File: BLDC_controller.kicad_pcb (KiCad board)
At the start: 4 copper layers, 50 x 38 mm, 368 parts, among them P2 CONN_01X06, P3 CONN_01X05, P5 CONN_01X05, Q1 PSMN2R0-30YLD, Q2 PSMN2R0-30YLD, Q3 PSMN2R0-30YLD, Q4 PSMN2R0-30YLD, Q5 PSMN2R0-30YLD, Q6 PSMN2R0-30YLD

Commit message: ready for 2nd review
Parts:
- moved REF** 0.35 mm to (178.3, 109.9)
- moved C19 0.32 mm to (176.8, 110.8)
- moved C5 0.30 mm to (176.7, 91.5)
- moved R14 0.25 mm to (163.5, 109.0)
- moved Q3 0.12 mm to (177.1, 105.4)
- moved Q5 0.08 mm to (177.1, 96.5)
- moved Q4 0.05 mm to (177.1, 105.4)
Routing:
- net +12V: track 32.3 -> 56.6 mm
- net /OUTU: track 47.4 -> 58.0 mm
- net /OUTW: track 32.9 -> 42.1 mm
- net /OUTV: track 29.1 -> 37.6 mm
- net GND: track 122.4 -> 118.4 mm
- net /LSW: track 21.0 -> 19.8 mm
- net /OSC_IN: track 7.60 -> 8.69 mm
- net /OP2P: track 6.87 -> 7.56 mm
- net +3V3: track 35.2 -> 34.6 mm
- net /V_ADC: track 18.7 -> 18.1 mm
- net /OP2N: track 13.4 -> 12.8 mm
- net /NRST: track 39.0 -> 38.5 mm
- net (no net): vias 4 -> 0

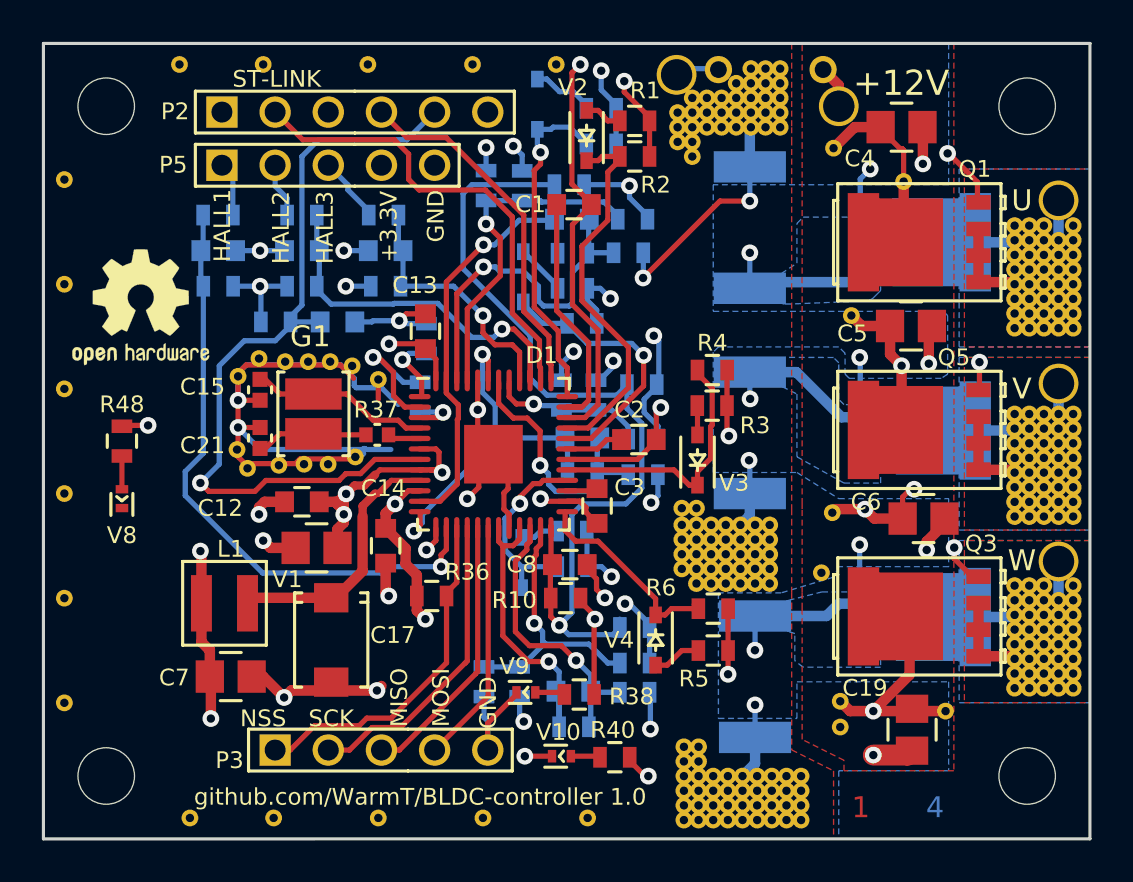
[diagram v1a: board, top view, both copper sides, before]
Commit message: board size changed to 49x32 mm
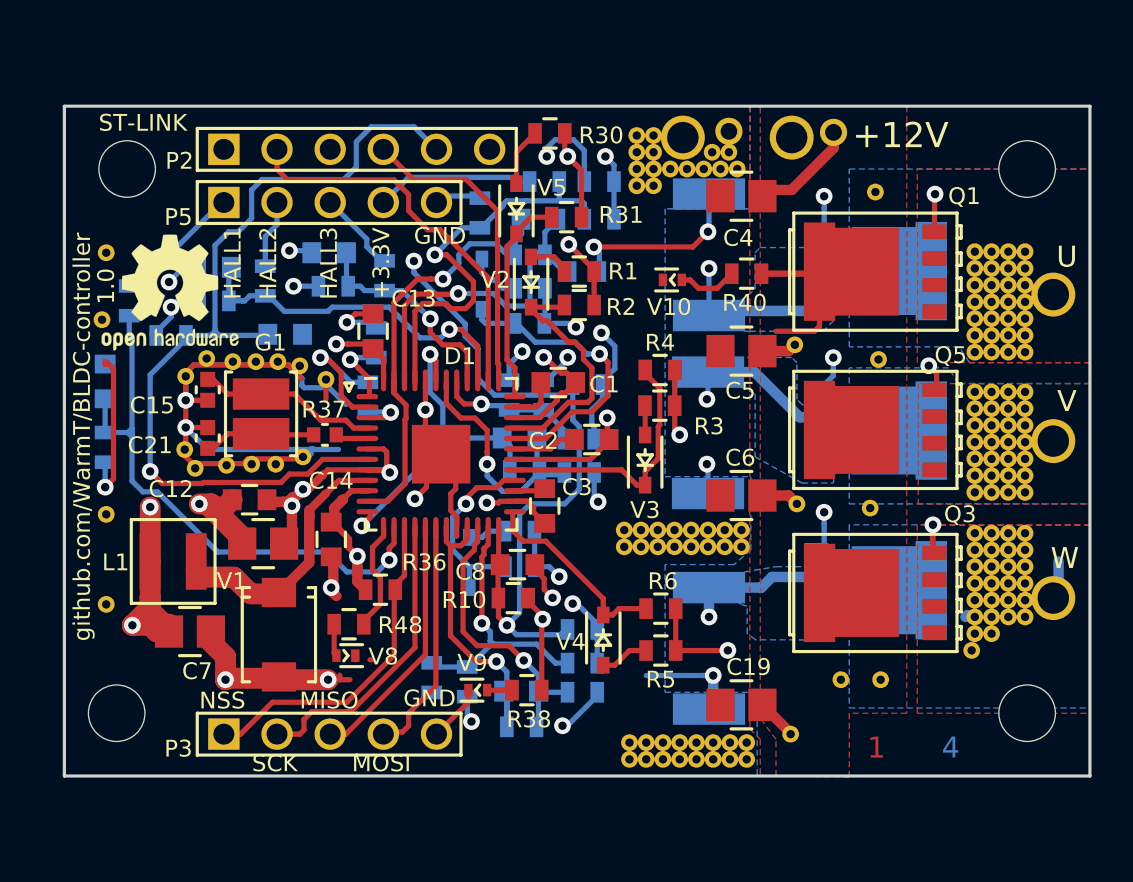
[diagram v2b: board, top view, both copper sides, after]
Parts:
- removed the REF** at (176.3, 84.6)
- removed the REF** at (183.8, 96.4)
- removed the REF** at (183.1, 96.4)
- removed the REF** at (182.3, 96.4)
- removed the REF** at (181.7, 96.4)
- removed the REF** at (184.4, 95.7)
- removed the REF** at (183.8, 95.7)
- removed the REF** at (183.1, 95.7)
- removed the REF** at (182.3, 95.7)
- removed the REF** at (181.7, 103.9)
- removed the REF** at (184.4, 91.6)
- removed the REF** at (161.2, 115.0)
- removed the REF** at (183.8, 91.6)
- removed the REF** at (183.1, 91.6)
- removed the REF** at (182.3, 91.6)
- removed the REF** at (181.7, 91.6)
- removed the REF** at (184.4, 90.9)
- removed the REF** at (183.8, 90.9)
- removed the REF** at (183.1, 90.9)
- removed the REF** at (182.3, 90.9)
- removed the REF** at (181.7, 90.9)
- removed the REF** at (184.4, 90.2)
- removed the REF** at (159.8, 79.0)
- removed the REF** at (183.8, 90.2)
- removed the REF** at (183.1, 90.2)
- removed the REF** at (182.3, 90.2)
- removed the REF** at (181.7, 90.2)
- removed the REF** at (184.4, 89.5)
- removed the REF** at (183.8, 89.5)
- removed the REF** at (183.1, 89.5)
- removed the REF** at (182.3, 89.5)
- removed the REF** at (181.7, 89.5)
- removed the REF** at (184.4, 88.8)
- removed the REF** at (136.2, 109.5)
- removed the REF** at (183.8, 88.8)
- removed the REF** at (183.1, 88.8)
- removed the REF** at (182.3, 88.8)
- removed the REF** at (181.7, 88.8)
- removed the REF** at (184.4, 88.1)
- removed the REF** at (183.8, 88.1)
- removed the REF** at (183.1, 88.1)
- removed the REF** at (182.3, 88.1)
- removed the REF** at (181.7, 88.1)
- removed the REF** at (184.4, 87.4)
- removed the REF** at (155.8, 79.0)
- removed the REF** at (183.8, 87.4)
- removed the REF** at (183.1, 87.4)
- removed the REF** at (182.3, 87.4)
- removed the REF** at (181.7, 87.4)
- removed the REF** at (181.7, 95.7)
- removed the REF** at (184.4, 86.7)
- removed the REF** at (183.1, 86.7)
- removed the REF** at (182.3, 86.7)
- removed the REF** at (181.7, 86.7)
- removed the REF** at (166.2, 83.4)
- removed the REF** at (150.8, 79.0)
- removed the REF** at (166.4, 100.2)
- removed the REF** at (165.8, 100.2)
- removed the REF** at (170.4, 82.0)
- removed the REF** at (169.8, 82.0)
- removed the REF** at (169.1, 82.0)
- removed the REF** at (168.3, 82.0)
- removed the REF** at (167.7, 82.0)
- removed the REF** at (166.9, 82.0)
- removed the REF** at (166.2, 82.0)
- removed the REF** at (165.6, 82.0)
- removed the REF** at (145.8, 79.0)
- removed the REF** at (170.4, 81.3)
- removed the REF** at (169.8, 81.3)
- removed the REF** at (169.1, 81.3)
- removed the REF** at (168.3, 81.3)
- removed the REF** at (167.7, 81.3)
- removed the REF** at (166.9, 81.3)
- removed the REF** at (166.2, 81.3)
- removed the REF** at (165.6, 81.3)
- removed the REF** at (170.4, 80.6)
- removed the REF** at (169.8, 80.6)
- removed the REF** at (141.8, 79.0)
- removed the REF** at (169.1, 80.6)
- removed the REF** at (168.3, 80.6)
- removed the REF** at (167.7, 80.6)
- removed the REF** at (166.9, 80.6)
- removed the REF** at (166.2, 80.6)
- removed the REF** at (170.4, 79.9)
- removed the REF** at (169.8, 79.9)
- removed the REF** at (169.1, 79.9)
- removed the REF** at (168.3, 79.9)
- removed the REF** at (166.2, 82.7)
- removed the REF** at (136.2, 84.5)
- removed the REF** at (165.6, 82.7)
- removed the REF** at (170.4, 79.2)
- removed the REF** at (169.8, 79.2)
- removed the REF** at (169.1, 79.2)
- removed the REF** at (166.6, 112.3)
- removed the REF** at (165.8, 112.3)
- removed the REF** at (166.6, 111.6)
- removed the REF** at (165.8, 111.6)
- removed the REF** at (169.9, 103.8)
- removed the REF** at (169.2, 103.8)
- removed the REF** at (168.6, 103.8)
- removed the REF** at (167.8, 103.8)
- removed the REF** at (167.2, 103.8)
- removed the REF** at (166.4, 103.8)
- removed the REF** at (169.9, 103.1)
- removed the REF** at (169.2, 103.1)
- removed the REF** at (168.6, 103.1)
- removed the REF** at (167.8, 103.1)
- removed the REF** at (167.2, 103.1)
- removed the REF** at (166.4, 103.1)
- removed the REF** at (169.9, 101.0)
- removed the REF** at (165.8, 103.1)
- removed the REF** at (169.9, 102.4)
- removed the REF** at (169.2, 102.4)
- removed the REF** at (168.6, 102.4)
- removed the REF** at (167.8, 102.4)
- removed the REF** at (167.2, 102.4)
- removed the REF** at (166.4, 102.4)
- removed the REF** at (165.8, 102.4)
- removed the REF** at (169.9, 101.7)
- removed the REF** at (169.2, 101.7)
- removed the REF** at (168.6, 101.7)
- removed the REF** at (167.8, 101.7)
- removed the REF** at (167.2, 101.7)
- removed the REF** at (166.4, 101.7)
- removed the REF** at (165.8, 101.7)
- removed the REF** at (169.2, 101.0)
- removed the REF** at (168.6, 101.0)
- removed the REF** at (167.8, 101.0)
- removed the REF** at (167.2, 101.0)
- removed the REF** at (165.8, 101.0)
- removed the REF** at (171.4, 115.1)
- removed the REF** at (170.8, 115.1)
- removed the REF** at (170.1, 115.1)
- removed the REF** at (169.3, 115.1)
- removed the REF** at (168.7, 115.1)
- removed the REF** at (167.9, 115.1)
- removed the REF** at (167.2, 115.1)
- removed the REF** at (166.6, 115.1)
- removed the REF** at (165.8, 115.1)
- removed the REF** at (142.2, 115.0)
- removed the REF** at (171.4, 114.4)
- removed the REF** at (170.8, 114.4)
- removed the REF** at (170.1, 114.4)
- removed the REF** at (169.3, 114.4)
- removed the REF** at (168.7, 114.4)
- removed the REF** at (167.9, 114.4)
- removed the REF** at (167.2, 114.4)
- removed the REF** at (166.6, 114.4)
- removed the REF** at (165.8, 114.4)
- removed the REF** at (171.4, 113.7)
- removed the REF** at (146.2, 115.0)
- removed the REF** at (170.8, 113.7)
- removed the REF** at (170.1, 113.7)
- removed the REF** at (169.3, 113.7)
- removed the REF** at (168.7, 113.7)
- removed the REF** at (167.9, 113.7)
- removed the REF** at (167.2, 113.7)
- removed the REF** at (166.6, 113.7)
- removed the REF** at (165.8, 113.7)
- removed the REF** at (171.4, 113.0)
- removed the REF** at (170.8, 113.0)
- removed the REF** at (151.2, 115.0)
- removed the REF** at (170.1, 113.0)
- removed the REF** at (169.3, 113.0)
- removed the REF** at (168.7, 113.0)
- removed the REF** at (167.9, 113.0)
- removed the REF** at (167.2, 113.0)
- removed the REF** at (166.6, 113.0)
- removed the REF** at (156.2, 115.0)
- removed the REF** at (173.0, 83.0)
- removed the REF** at (172.9, 100.4)
- removed the REF** at (172.4, 103.3)
- removed the REF** at (173.8, 91.0)
- removed the REF** at (173.3, 110.7)
- removed the REF** at (184.4, 108.8)
- removed the REF** at (183.8, 108.8)
- removed the REF** at (183.1, 108.8)
- removed the REF** at (182.3, 108.8)
- removed the REF** at (181.7, 108.8)
- removed the REF** at (184.4, 108.1)
- removed the REF** at (183.8, 108.1)
- removed the REF** at (183.1, 108.1)
- removed the REF** at (182.3, 108.1)
- removed the REF** at (181.7, 108.1)
- removed the REF** at (184.4, 107.4)
- removed the REF** at (183.8, 107.4)
- removed the REF** at (183.1, 107.4)
- removed the REF** at (182.3, 107.4)
- removed the REF** at (181.7, 107.4)
- removed the REF** at (184.4, 106.7)
- removed the REF** at (183.8, 106.7)
- removed the REF** at (183.1, 106.7)
- removed the REF** at (182.3, 106.7)
- removed the REF** at (181.7, 106.7)
- removed the REF** at (184.4, 106.0)
- removed the REF** at (183.8, 106.0)
- removed the REF** at (183.1, 106.0)
- removed the REF** at (182.3, 106.0)
- removed the REF** at (181.7, 106.0)
- removed the REF** at (184.4, 105.3)
- removed the REF** at (183.8, 105.3)
- removed the REF** at (183.1, 105.3)
- removed the REF** at (182.3, 105.3)
- removed the REF** at (181.7, 105.3)
- removed the REF** at (184.4, 104.6)
- removed the REF** at (183.8, 104.6)
- removed the REF** at (183.1, 104.6)
- removed the REF** at (182.3, 104.6)
- removed the REF** at (181.7, 104.6)
- removed the REF** at (184.4, 103.9)
- removed the REF** at (183.1, 103.9)
- removed the REF** at (182.3, 103.9)
- removed the REF** at (184.4, 100.6)
- removed the REF** at (183.8, 100.6)
- removed the REF** at (183.1, 100.6)
- removed the REF** at (182.3, 100.6)
- removed the REF** at (181.7, 100.6)
- removed the REF** at (184.4, 99.9)
- removed the REF** at (183.8, 99.9)
- removed the REF** at (183.1, 99.9)
- removed the REF** at (182.3, 99.9)
- removed the REF** at (181.7, 99.9)
- removed the REF** at (184.4, 99.2)
- removed the REF** at (178.3, 109.9)
- removed the REF** at (183.8, 99.2)
- removed the REF** at (183.1, 99.2)
- removed the REF** at (182.3, 99.2)
- removed the REF** at (181.7, 99.2)
- removed the REF** at (184.4, 98.5)
- removed the REF** at (183.8, 98.5)
- removed the REF** at (183.1, 98.5)
- removed the REF** at (182.3, 98.5)
- removed the REF** at (181.7, 98.5)
- removed the REF** at (184.4, 97.8)
- removed the REF** at (173.3, 109.4)
- removed the REF** at (183.8, 97.8)
- removed the REF** at (183.1, 97.8)
- removed the REF** at (182.3, 97.8)
- removed the REF** at (181.7, 97.8)
- removed the REF** at (184.4, 97.1)
- removed the REF** at (183.8, 97.1)
- removed the REF** at (183.1, 97.1)
- removed the REF** at (182.3, 97.1)
- removed the REF** at (181.7, 97.1)
- removed the REF** at (184.4, 96.4)
- added REF**: VIA-0.8mm-0.4mm, project_footprints:VIA-0.8mm-0.4mm, F.Cu at (175.0, 85.1)
- added REF**: VIA-0.8mm-0.4mm, project_footprints:VIA-0.8mm-0.4mm, F.Cu at (168.4, 84.0)
- added REF**: VIA-0.8mm-0.4mm, project_footprints:VIA-0.8mm-0.4mm, F.Cu at (179.8, 103.8)
- added REF**: VIA-0.8mm-0.4mm, project_footprints:VIA-0.8mm-0.4mm, F.Cu at (182.2, 103.0)
- added REF**: VIA-0.8mm-0.4mm, project_footprints:VIA-0.8mm-0.4mm, F.Cu at (181.3, 103.0)
- added REF**: VIA-0.8mm-0.4mm, project_footprints:VIA-0.8mm-0.4mm, F.Cu at (180.6, 103.0)
- added REF**: VIA-0.8mm-0.4mm, project_footprints:VIA-0.8mm-0.4mm, F.Cu at (179.8, 103.0)
- added REF**: VIA-0.8mm-0.4mm, project_footprints:VIA-0.8mm-0.4mm, F.Cu at (182.2, 102.2)
- added REF**: VIA-0.8mm-0.4mm, project_footprints:VIA-0.8mm-0.4mm, F.Cu at (181.3, 102.2)
- added REF**: VIA-0.8mm-0.4mm, project_footprints:VIA-0.8mm-0.4mm, F.Cu at (180.6, 102.2)
- added REF**: VIA-0.8mm-0.4mm, project_footprints:VIA-0.8mm-0.4mm, F.Cu at (179.8, 102.2)
- added REF**: VIA-0.8mm-0.4mm, project_footprints:VIA-0.8mm-0.4mm, F.Cu at (182.2, 101.4)
- added REF**: VIA-0.8mm-0.4mm, project_footprints:VIA-0.8mm-0.4mm, F.Cu at (167.6, 84.0)
- added REF**: VIA-0.8mm-0.4mm, project_footprints:VIA-0.8mm-0.4mm, F.Cu at (181.3, 101.4)
- added REF**: VIA-0.8mm-0.4mm, project_footprints:VIA-0.8mm-0.4mm, F.Cu at (180.6, 101.4)
- added REF**: VIA-0.8mm-0.4mm, project_footprints:VIA-0.8mm-0.4mm, F.Cu at (168.8, 112.2)
- added REF**: VIA-0.8mm-0.4mm, project_footprints:VIA-0.8mm-0.4mm, F.Cu at (168.1, 112.2)
- added REF**: VIA-0.8mm-0.4mm, project_footprints:VIA-0.8mm-0.4mm, F.Cu at (167.2, 112.2)
- added REF**: VIA-0.8mm-0.4mm, project_footprints:VIA-0.8mm-0.4mm, F.Cu at (166.4, 112.2)
- added REF**: VIA-0.8mm-0.4mm, project_footprints:VIA-0.8mm-0.4mm, F.Cu at (165.7, 112.2)
- added REF**: VIA-0.8mm-0.4mm, project_footprints:VIA-0.8mm-0.4mm, F.Cu at (164.8, 112.2)
- added REF**: VIA-0.8mm-0.4mm, project_footprints:VIA-0.8mm-0.4mm, F.Cu at (164.1, 112.2)
- added REF**: VIA-0.8mm-0.4mm, project_footprints:VIA-0.8mm-0.4mm, F.Cu at (163.2, 112.2)
- added REF**: VIA-0.8mm-0.4mm, project_footprints:VIA-0.8mm-0.4mm, F.Cu at (166.8, 84.0)
- added REF**: VIA-0.8mm-0.4mm, project_footprints:VIA-0.8mm-0.4mm, F.Cu at (168.8, 111.4)
- added REF**: VIA-0.8mm-0.4mm, project_footprints:VIA-0.8mm-0.4mm, F.Cu at (168.1, 111.4)
- added REF**: VIA-0.8mm-0.4mm, project_footprints:VIA-0.8mm-0.4mm, F.Cu at (167.2, 111.4)
- added REF**: VIA-0.8mm-0.4mm, project_footprints:VIA-0.8mm-0.4mm, F.Cu at (166.4, 111.4)
- added REF**: VIA-0.8mm-0.4mm, project_footprints:VIA-0.8mm-0.4mm, F.Cu at (165.7, 111.4)
- added REF**: VIA-0.8mm-0.4mm, project_footprints:VIA-0.8mm-0.4mm, F.Cu at (164.8, 111.4)
- added REF**: VIA-0.8mm-0.4mm, project_footprints:VIA-0.8mm-0.4mm, F.Cu at (164.1, 111.4)
- added REF**: VIA-0.8mm-0.4mm, project_footprints:VIA-0.8mm-0.4mm, F.Cu at (170.9, 111.0)
- added REF**: VIA-0.8mm-0.4mm, project_footprints:VIA-0.8mm-0.4mm, F.Cu at (173.3, 108.4)
- added REF**: VIA-0.8mm-0.4mm, project_footprints:VIA-0.8mm-0.4mm, F.Cu at (175.2, 108.4)
- added REF**: VIA-0.8mm-0.4mm, project_footprints:VIA-0.8mm-0.4mm, F.Cu at (166.0, 84.0)
- added REF**: VIA-0.8mm-0.4mm, project_footprints:VIA-0.8mm-0.4mm, F.Cu at (174.8, 100.2)
- added REF**: VIA-0.8mm-0.4mm, project_footprints:VIA-0.8mm-0.4mm, F.Cu at (175.2, 93.1)
- added REF**: VIA-0.8mm-0.4mm, project_footprints:VIA-0.8mm-0.4mm, F.Cu at (171.2, 92.4)
- added REF**: VIA-0.8mm-0.4mm, project_footprints:VIA-0.8mm-0.4mm, F.Cu at (171.2, 100.0)
- added REF**: VIA-0.8mm-0.4mm, project_footprints:VIA-0.8mm-0.4mm, F.Cu at (179.8, 101.4)
- added REF**: VIA-0.8mm-0.4mm, project_footprints:VIA-0.8mm-0.4mm, F.Cu at (179.8, 94.7)
- added REF**: VIA-0.8mm-0.4mm, project_footprints:VIA-0.8mm-0.4mm, F.Cu at (179.8, 88.0)
- added REF**: VIA-0.8mm-0.4mm, project_footprints:VIA-0.8mm-0.4mm, F.Cu at (165.2, 84.0)
- added REF**: VIA-0.8mm-0.4mm, project_footprints:VIA-0.8mm-0.4mm, F.Cu at (164.4, 84.0)
- added REF**: VIA-0.8mm-0.4mm, project_footprints:VIA-0.8mm-0.4mm, F.Cu at (163.6, 84.0)
- added REF**: VIA-0.8mm-0.4mm, project_footprints:VIA-0.8mm-0.4mm, F.Cu at (168.6, 102.0)
- added REF**: VIA-0.8mm-0.4mm, project_footprints:VIA-0.8mm-0.4mm, F.Cu at (167.8, 102.0)
- added REF**: VIA-0.8mm-0.4mm, project_footprints:VIA-0.8mm-0.4mm, F.Cu at (167.0, 102.0)
- added REF**: VIA-0.8mm-0.4mm, project_footprints:VIA-0.8mm-0.4mm, F.Cu at (164.4, 82.4)
- added REF**: VIA-0.8mm-0.4mm, project_footprints:VIA-0.8mm-0.4mm, F.Cu at (166.2, 102.0)
- added REF**: VIA-0.8mm-0.4mm, project_footprints:VIA-0.8mm-0.4mm, F.Cu at (165.4, 102.0)
- added REF**: VIA-0.8mm-0.4mm, project_footprints:VIA-0.8mm-0.4mm, F.Cu at (164.6, 102.0)
- added REF**: VIA-0.8mm-0.4mm, project_footprints:VIA-0.8mm-0.4mm, F.Cu at (163.8, 102.0)
- added REF**: VIA-0.8mm-0.4mm, project_footprints:VIA-0.8mm-0.4mm, F.Cu at (163.0, 102.0)
- added REF**: VIA-0.8mm-0.4mm, project_footprints:VIA-0.8mm-0.4mm, F.Cu at (168.6, 101.2)
- added REF**: VIA-0.8mm-0.4mm, project_footprints:VIA-0.8mm-0.4mm, F.Cu at (167.8, 101.2)
- added REF**: VIA-0.8mm-0.4mm, project_footprints:VIA-0.8mm-0.4mm, F.Cu at (167.0, 101.2)
- added REF**: VIA-0.8mm-0.4mm, project_footprints:VIA-0.8mm-0.4mm, F.Cu at (166.2, 101.2)
- added REF**: VIA-0.8mm-0.4mm, project_footprints:VIA-0.8mm-0.4mm, F.Cu at (165.4, 101.2)
- added REF**: VIA-0.8mm-0.4mm, project_footprints:VIA-0.8mm-0.4mm, F.Cu at (163.6, 82.4)
- added REF**: VIA-0.8mm-0.4mm, project_footprints:VIA-0.8mm-0.4mm, F.Cu at (164.6, 101.2)
- added REF**: VIA-0.8mm-0.4mm, project_footprints:VIA-0.8mm-0.4mm, F.Cu at (163.8, 101.2)
- added REF**: VIA-0.8mm-0.4mm, project_footprints:VIA-0.8mm-0.4mm, F.Cu at (182.2, 99.5)
- added REF**: VIA-0.8mm-0.4mm, project_footprints:VIA-0.8mm-0.4mm, F.Cu at (181.3, 99.5)
- added REF**: VIA-0.8mm-0.4mm, project_footprints:VIA-0.8mm-0.4mm, F.Cu at (180.6, 99.5)
- added REF**: VIA-0.8mm-0.4mm, project_footprints:VIA-0.8mm-0.4mm, F.Cu at (179.8, 99.5)
- added REF**: VIA-0.8mm-0.4mm, project_footprints:VIA-0.8mm-0.4mm, F.Cu at (182.2, 98.7)
- added REF**: VIA-0.8mm-0.4mm, project_footprints:VIA-0.8mm-0.4mm, F.Cu at (181.3, 98.7)
- added REF**: VIA-0.8mm-0.4mm, project_footprints:VIA-0.8mm-0.4mm, F.Cu at (180.6, 98.7)
- added REF**: VIA-0.8mm-0.4mm, project_footprints:VIA-0.8mm-0.4mm, F.Cu at (179.8, 98.7)
- added REF**: VIA-0.8mm-0.4mm, project_footprints:VIA-0.8mm-0.4mm, F.Cu at (163.6, 83.2)
- added REF**: VIA-0.8mm-0.4mm, project_footprints:VIA-0.8mm-0.4mm, F.Cu at (182.2, 97.8)
- added REF**: VIA-0.8mm-0.4mm, project_footprints:VIA-0.8mm-0.4mm, F.Cu at (181.3, 97.8)
- added REF**: VIA-0.8mm-0.4mm, project_footprints:VIA-0.8mm-0.4mm, F.Cu at (180.6, 97.8)
- added REF**: VIA-0.8mm-0.4mm, project_footprints:VIA-0.8mm-0.4mm, F.Cu at (179.8, 97.8)
- added REF**: VIA-0.8mm-0.4mm, project_footprints:VIA-0.8mm-0.4mm, F.Cu at (182.2, 97.0)
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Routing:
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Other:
- board size 50 x 38 mm -> 49 x 32 mm
- board text added: "1.0"
- board text added: "github.com/WarmT/BLDC-controller"
- board text removed: "github.com/WarmT/BLDC-controller 1.0"

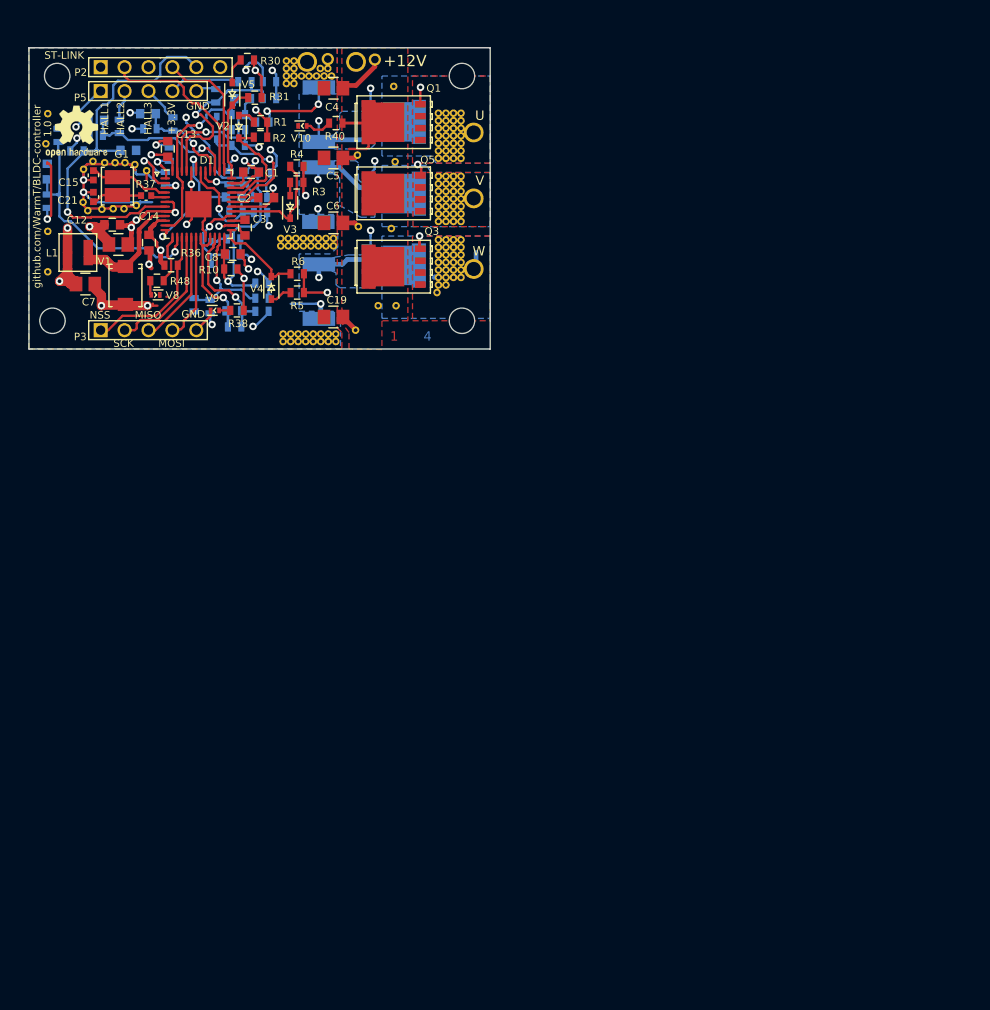
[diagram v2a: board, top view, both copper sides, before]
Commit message: panelize design
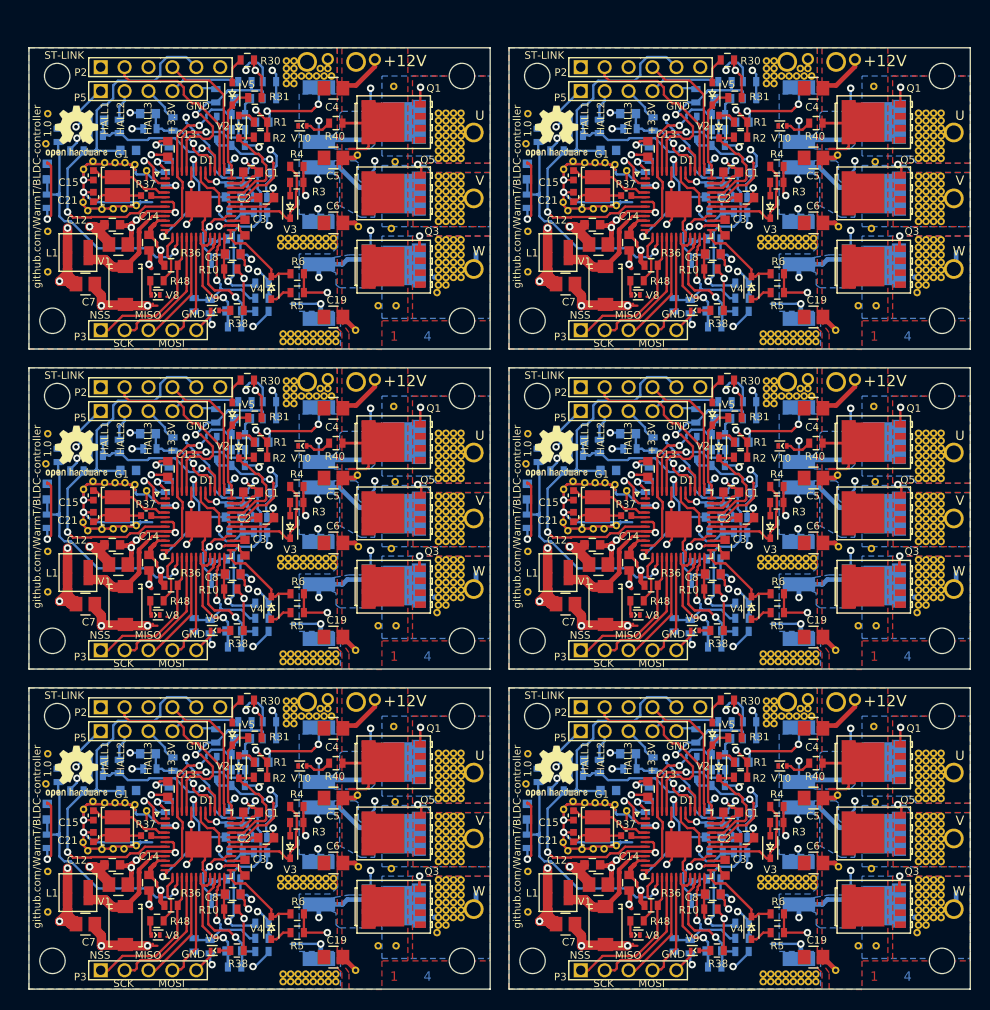
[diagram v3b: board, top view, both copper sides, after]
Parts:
- added C1: 100n, project_footprints:C_0603, F.Cu at (210.8, 162.2)
- added C1: 100n, project_footprints:C_0603, F.Cu at (159.8, 162.2)
- added C1: 100n, project_footprints:C_0603, F.Cu at (210.8, 128.2)
- added C1: 100n, project_footprints:C_0603, F.Cu at (159.8, 128.2)
- added C1: 100n, project_footprints:C_0603, F.Cu at (210.8, 94.2)
- added C10: 100p, project_footprints:C_0603, B.Cu at (209.0, 164.8)
- added C10: 100p, project_footprints:C_0603, B.Cu at (158.0, 164.8)
- added C10: 100p, project_footprints:C_0603, B.Cu at (209.0, 130.8)
- added C10: 100p, project_footprints:C_0603, B.Cu at (158.0, 130.8)
- added C10: 100p, project_footprints:C_0603, B.Cu at (209.0, 96.8)
- added C11: 100p, project_footprints:C_0603, B.Cu at (209.9, 154.4)
- added C11: 100p, project_footprints:C_0603, B.Cu at (158.9, 154.4)
- added C11: 100p, project_footprints:C_0603, B.Cu at (209.9, 120.4)
- added C11: 100p, project_footprints:C_0603, B.Cu at (158.9, 120.4)
- added C11: 100p, project_footprints:C_0603, B.Cu at (209.9, 86.4)
- added C12: 100n, project_footprints:C_0603, F.Cu at (196.1, 167.8)
- added C12: 100n, project_footprints:C_0603, F.Cu at (145.1, 167.8)
- added C12: 100n, project_footprints:C_0603, F.Cu at (196.1, 133.8)
- added C12: 100n, project_footprints:C_0603, F.Cu at (145.1, 133.8)
- added C12: 100n, project_footprints:C_0603, F.Cu at (196.1, 99.8)
- added C13: 100n, project_footprints:C_0603, F.Cu at (202.0, 159.8)
- added C13: 100n, project_footprints:C_0603, F.Cu at (151.0, 159.8)
- added C13: 100n, project_footprints:C_0603, F.Cu at (202.0, 125.8)
- added C13: 100n, project_footprints:C_0603, F.Cu at (151.0, 125.8)
- added C13: 100n, project_footprints:C_0603, F.Cu at (202.0, 91.8)
- added C14: 100n, project_footprints:C_0603, F.Cu at (200.0, 169.7)
- added C14: 100n, project_footprints:C_0603, F.Cu at (149.0, 169.7)
- added C14: 100n, project_footprints:C_0603, F.Cu at (200.0, 135.7)
- added C14: 100n, project_footprints:C_0603, F.Cu at (149.0, 135.7)
- added C14: 100n, project_footprints:C_0603, F.Cu at (200.0, 101.7)
- added C15: 10p, project_footprints:C_0402, F.Cu at (194.1, 162.6)
- added C15: 10p, project_footprints:C_0402, F.Cu at (143.1, 162.6)
- added C15: 10p, project_footprints:C_0402, F.Cu at (194.1, 128.6)
- added C15: 10p, project_footprints:C_0402, F.Cu at (143.1, 128.6)
- added C15: 10p, project_footprints:C_0402, F.Cu at (194.1, 94.5)
- added C16: 3n3, project_footprints:C_0603, B.Cu at (197.8, 159.9)
- added C16: 3n3, project_footprints:C_0603, B.Cu at (146.8, 159.9)
- added C16: 3n3, project_footprints:C_0603, B.Cu at (197.8, 125.9)
- added C16: 3n3, project_footprints:C_0603, B.Cu at (146.8, 125.9)
- added C16: 3n3, project_footprints:C_0603, B.Cu at (197.8, 91.9)
- added C17: 220n, project_footprints:C_0805, F.Cu at (196.8, 169.9)
- added C17: 220n, project_footprints:C_0805, F.Cu at (145.8, 169.9)
- added C17: 220n, project_footprints:C_0805, F.Cu at (196.8, 135.9)
- added C17: 220n, project_footprints:C_0805, F.Cu at (145.8, 135.9)
- added C17: 220n, project_footprints:C_0805, F.Cu at (196.8, 101.9)
- added C19: 220n, project_footprints:C_0805, F.Cu at (219.6, 177.6)
- added C19: 220n, project_footprints:C_0805, F.Cu at (168.6, 177.6)
- added C19: 220n, project_footprints:C_0805, F.Cu at (219.6, 143.6)
- added C19: 220n, project_footprints:C_0805, F.Cu at (168.6, 143.6)
- added C19: 220n, project_footprints:C_0805, F.Cu at (219.6, 109.6)
- added C2: 100n, project_footprints:C_0603, F.Cu at (212.4, 164.9)
- added C2: 100n, project_footprints:C_0603, F.Cu at (161.4, 164.9)
- added C2: 100n, project_footprints:C_0603, F.Cu at (212.4, 130.9)
- added C2: 100n, project_footprints:C_0603, F.Cu at (161.4, 130.9)
- added C2: 100n, project_footprints:C_0603, F.Cu at (212.4, 96.9)
- added C21: 10p, project_footprints:C_0402, F.Cu at (194.1, 164.8)
- added C21: 10p, project_footprints:C_0402, F.Cu at (143.1, 164.8)
- added C21: 10p, project_footprints:C_0402, F.Cu at (194.1, 130.8)
- added C21: 10p, project_footprints:C_0402, F.Cu at (143.1, 130.8)
- added C21: 10p, project_footprints:C_0402, F.Cu at (194.1, 96.8)
- added C22: 10p, project_footprints:C_0603, B.Cu at (189.2, 162.2)
- added C22: 10p, project_footprints:C_0603, B.Cu at (138.2, 162.2)
- added C22: 10p, project_footprints:C_0603, B.Cu at (189.2, 128.2)
- added C22: 10p, project_footprints:C_0603, B.Cu at (138.2, 128.2)
- added C22: 10p, project_footprints:C_0603, B.Cu at (189.2, 94.2)
- added C23: 10p, project_footprints:C_0603, B.Cu at (194.4, 156.7)
- added C23: 10p, project_footprints:C_0603, B.Cu at (143.4, 156.7)
- added C23: 10p, project_footprints:C_0603, B.Cu at (194.4, 122.7)
- added C23: 10p, project_footprints:C_0603, B.Cu at (143.4, 122.7)
- added C23: 10p, project_footprints:C_0603, B.Cu at (194.4, 88.7)
- added C24: 10p, project_footprints:C_0603, B.Cu at (199.9, 156.0)
- added C24: 10p, project_footprints:C_0603, B.Cu at (148.9, 156.0)
- added C24: 10p, project_footprints:C_0603, B.Cu at (199.9, 122.0)
- added C24: 10p, project_footprints:C_0603, B.Cu at (148.9, 122.0)
- added C24: 10p, project_footprints:C_0603, B.Cu at (199.9, 88.0)
- added C3: 100n, project_footprints:C_0603, F.Cu at (210.2, 168.1)
- added C3: 100n, project_footprints:C_0603, F.Cu at (159.2, 168.1)
- added C3: 100n, project_footprints:C_0603, F.Cu at (210.2, 134.1)
- added C3: 100n, project_footprints:C_0603, F.Cu at (159.2, 134.1)
- added C3: 100n, project_footprints:C_0603, F.Cu at (210.2, 100.1)
- added C4: 220n, project_footprints:C_0805, F.Cu at (219.6, 153.3)
- added C4: 220n, project_footprints:C_0805, F.Cu at (168.6, 153.3)
- added C4: 220n, project_footprints:C_0805, F.Cu at (219.6, 119.3)
- added C4: 220n, project_footprints:C_0805, F.Cu at (168.6, 119.3)
- added C4: 220n, project_footprints:C_0805, F.Cu at (219.6, 85.3)
- added C5: 220n, project_footprints:C_0805, F.Cu at (219.6, 160.7)
- added C5: 220n, project_footprints:C_0805, F.Cu at (168.6, 160.7)
- added C5: 220n, project_footprints:C_0805, F.Cu at (219.6, 126.7)
- added C5: 220n, project_footprints:C_0805, F.Cu at (168.6, 126.7)
- added C5: 220n, project_footprints:C_0805, F.Cu at (219.6, 92.7)
- added C6: 220n, project_footprints:C_0805, F.Cu at (219.6, 167.6)
- added C6: 220n, project_footprints:C_0805, F.Cu at (168.6, 167.6)
- added C6: 220n, project_footprints:C_0805, F.Cu at (219.6, 133.6)
- added C6: 220n, project_footprints:C_0805, F.Cu at (168.6, 133.6)
- added C6: 220n, project_footprints:C_0805, F.Cu at (219.6, 99.6)
- added C7: 47u, project_footprints:C_0805, F.Cu at (193.2, 174.1)
- added C7: 47u, project_footprints:C_0805, F.Cu at (142.2, 174.1)
- added C7: 47u, project_footprints:C_0805, F.Cu at (193.2, 140.1)
- added C7: 47u, project_footprints:C_0805, F.Cu at (142.2, 140.1)
- added C7: 47u, project_footprints:C_0805, F.Cu at (193.2, 106.1)
- added C8: 1n0, project_footprints:C_0603, F.Cu at (208.9, 170.9)
- added C8: 1n0, project_footprints:C_0603, F.Cu at (157.9, 170.9)
- added C8: 1n0, project_footprints:C_0603, F.Cu at (208.9, 136.9)
- added C8: 1n0, project_footprints:C_0603, F.Cu at (157.9, 136.9)
- added C8: 1n0, project_footprints:C_0603, F.Cu at (208.9, 102.9)
- added C9: 100p, project_footprints:C_0603, B.Cu at (209.1, 176.9)
- added C9: 100p, project_footprints:C_0603, B.Cu at (158.1, 176.9)
- added C9: 100p, project_footprints:C_0603, B.Cu at (209.1, 142.9)
- added C9: 100p, project_footprints:C_0603, B.Cu at (158.1, 142.9)
- added C9: 100p, project_footprints:C_0603, B.Cu at (209.1, 109.0)
- added D1: STSPIN32F0, project_footprints:QFN-48-1EP_7x7mm_Pitch0.5mm, F.Cu at (205.2, 165.6)
- added D1: STSPIN32F0, project_footprints:QFN-48-1EP_7x7mm_Pitch0.5mm, F.Cu at (154.2, 165.6)
- added D1: STSPIN32F0, project_footprints:QFN-48-1EP_7x7mm_Pitch0.5mm, F.Cu at (205.2, 131.6)
- added D1: STSPIN32F0, project_footprints:QFN-48-1EP_7x7mm_Pitch0.5mm, F.Cu at (154.2, 131.6)
- added D1: STSPIN32F0, project_footprints:QFN-48-1EP_7x7mm_Pitch0.5mm, F.Cu at (205.2, 97.6)
- added G1: NX3225GD, project_footprints:Crystal_3225, F.Cu at (196.7, 163.7)
- added G1: NX3225GD, project_footprints:Crystal_3225, F.Cu at (145.7, 163.7)
- added G1: NX3225GD, project_footprints:Crystal_3225, F.Cu at (196.7, 129.7)
- added G1: NX3225GD, project_footprints:Crystal_3225, F.Cu at (145.7, 129.7)
- added G1: NX3225GD, project_footprints:Crystal_3225, F.Cu at (196.7, 95.7)
- added L1: SRN3015-220M, project_footprints:BOURNS-SRN3015, F.Cu at (192.4, 170.8)
- added L1: SRN3015-220M, project_footprints:BOURNS-SRN3015, F.Cu at (141.4, 170.8)
- added L1: SRN3015-220M, project_footprints:BOURNS-SRN3015, F.Cu at (192.4, 136.8)
- added L1: SRN3015-220M, project_footprints:BOURNS-SRN3015, F.Cu at (141.4, 136.8)
- added L1: SRN3015-220M, project_footprints:BOURNS-SRN3015, F.Cu at (192.4, 102.8)
- added P2: CONN_01X06, project_footprints:PINHEAD1-6, F.Cu at (201.2, 151.1)
- added P2: CONN_01X06, project_footprints:PINHEAD1-6, F.Cu at (150.2, 151.1)
- added P2: CONN_01X06, project_footprints:PINHEAD1-6, F.Cu at (201.2, 117.1)
- added P2: CONN_01X06, project_footprints:PINHEAD1-6, F.Cu at (150.2, 117.1)
- added P2: CONN_01X06, project_footprints:PINHEAD1-6, F.Cu at (201.2, 83.1)
- added P3: CONN_01X05, project_footprints:PINHEAD1-5, F.Cu at (199.9, 179.0)
- added P3: CONN_01X05, project_footprints:PINHEAD1-5, F.Cu at (148.9, 179.0)
- added P3: CONN_01X05, project_footprints:PINHEAD1-5, F.Cu at (199.9, 145.0)
- added P3: CONN_01X05, project_footprints:PINHEAD1-5, F.Cu at (148.9, 145.0)
- added P3: CONN_01X05, project_footprints:PINHEAD1-5, F.Cu at (199.9, 111.0)
- added P5: CONN_01X05, project_footprints:PINHEAD1-5, F.Cu at (199.9, 153.6)
- added P5: CONN_01X05, project_footprints:PINHEAD1-5, F.Cu at (148.9, 153.6)
- added P5: CONN_01X05, project_footprints:PINHEAD1-5, F.Cu at (199.9, 119.6)
- added P5: CONN_01X05, project_footprints:PINHEAD1-5, F.Cu at (148.9, 119.6)
- added P5: CONN_01X05, project_footprints:PINHEAD1-5, F.Cu at (199.9, 85.6)
- added Q1: PSMN2R0-30YLD, project_footprints:SOT-669_LFPAK56, F.Cu at (226.0, 156.9)
- added Q1: PSMN2R0-30YLD, project_footprints:SOT-669_LFPAK56, F.Cu at (175.0, 156.9)
- added Q1: PSMN2R0-30YLD, project_footprints:SOT-669_LFPAK56, F.Cu at (226.0, 122.9)
- added Q1: PSMN2R0-30YLD, project_footprints:SOT-669_LFPAK56, F.Cu at (175.0, 122.9)
- added Q1: PSMN2R0-30YLD, project_footprints:SOT-669_LFPAK56, F.Cu at (226.0, 88.9)
- added Q2: PSMN2R0-30YLD, project_footprints:SOT-669_LFPAK56, B.Cu at (226.0, 156.9)
- added Q2: PSMN2R0-30YLD, project_footprints:SOT-669_LFPAK56, B.Cu at (175.0, 156.9)
- added Q2: PSMN2R0-30YLD, project_footprints:SOT-669_LFPAK56, B.Cu at (226.0, 122.9)
- added Q2: PSMN2R0-30YLD, project_footprints:SOT-669_LFPAK56, B.Cu at (175.0, 122.9)
- added Q2: PSMN2R0-30YLD, project_footprints:SOT-669_LFPAK56, B.Cu at (226.0, 88.9)
- added Q3: PSMN2R0-30YLD, project_footprints:SOT-669_LFPAK56, F.Cu at (226.0, 172.3)
- added Q3: PSMN2R0-30YLD, project_footprints:SOT-669_LFPAK56, F.Cu at (175.0, 172.3)
- added Q3: PSMN2R0-30YLD, project_footprints:SOT-669_LFPAK56, F.Cu at (226.0, 138.3)
- added Q3: PSMN2R0-30YLD, project_footprints:SOT-669_LFPAK56, F.Cu at (175.0, 138.3)
- added Q3: PSMN2R0-30YLD, project_footprints:SOT-669_LFPAK56, F.Cu at (226.0, 104.3)
- added Q4: PSMN2R0-30YLD, project_footprints:SOT-669_LFPAK56, B.Cu at (226.0, 172.1)
- added Q4: PSMN2R0-30YLD, project_footprints:SOT-669_LFPAK56, B.Cu at (175.0, 172.1)
- added Q4: PSMN2R0-30YLD, project_footprints:SOT-669_LFPAK56, B.Cu at (226.0, 138.1)
- added Q4: PSMN2R0-30YLD, project_footprints:SOT-669_LFPAK56, B.Cu at (175.0, 138.1)
- added Q4: PSMN2R0-30YLD, project_footprints:SOT-669_LFPAK56, B.Cu at (226.0, 104.1)
- added Q5: PSMN2R0-30YLD, project_footprints:SOT-669_LFPAK56, F.Cu at (226.0, 164.5)
- added Q5: PSMN2R0-30YLD, project_footprints:SOT-669_LFPAK56, F.Cu at (175.0, 164.5)
- added Q5: PSMN2R0-30YLD, project_footprints:SOT-669_LFPAK56, F.Cu at (226.0, 130.5)
- added Q5: PSMN2R0-30YLD, project_footprints:SOT-669_LFPAK56, F.Cu at (175.0, 130.5)
- added Q5: PSMN2R0-30YLD, project_footprints:SOT-669_LFPAK56, F.Cu at (226.0, 96.5)
- added Q6: PSMN2R0-30YLD, project_footprints:SOT-669_LFPAK56, B.Cu at (226.0, 164.5)
- added Q6: PSMN2R0-30YLD, project_footprints:SOT-669_LFPAK56, B.Cu at (175.0, 164.5)
- added Q6: PSMN2R0-30YLD, project_footprints:SOT-669_LFPAK56, B.Cu at (226.0, 130.5)
- added Q6: PSMN2R0-30YLD, project_footprints:SOT-669_LFPAK56, B.Cu at (175.0, 130.5)
- added Q6: PSMN2R0-30YLD, project_footprints:SOT-669_LFPAK56, B.Cu at (226.0, 96.5)
- added R1: 10R, project_footprints:R_0603, F.Cu at (211.8, 156.9)
- added R1: 10R, project_footprints:R_0603, F.Cu at (160.8, 156.9)
- added R1: 10R, project_footprints:R_0603, F.Cu at (211.8, 122.9)
- added R1: 10R, project_footprints:R_0603, F.Cu at (160.8, 122.9)
- added R1: 10R, project_footprints:R_0603, F.Cu at (211.8, 88.9)
- added R10: 46k4, project_footprints:R_0603, F.Cu at (208.7, 172.5)
- added R10: 46k4, project_footprints:R_0603, F.Cu at (157.7, 172.5)
- added R10: 46k4, project_footprints:R_0603, F.Cu at (208.7, 138.5)
- added R10: 46k4, project_footprints:R_0603, F.Cu at (157.7, 138.5)
- added R10: 46k4, project_footprints:R_0603, F.Cu at (208.7, 104.5)
- added R11: 2k2, project_footprints:R_0603, B.Cu at (212.0, 174.0)
- added R11: 2k2, project_footprints:R_0603, B.Cu at (161.0, 174.0)
- added R11: 2k2, project_footprints:R_0603, B.Cu at (212.0, 140.0)
- added R11: 2k2, project_footprints:R_0603, B.Cu at (161.0, 140.0)
- added R11: 2k2, project_footprints:R_0603, B.Cu at (212.0, 106.0)
- added R12: 2k2, project_footprints:R_0603, B.Cu at (212.2, 162.3)
- added R12: 2k2, project_footprints:R_0603, B.Cu at (161.2, 162.3)
- added R12: 2k2, project_footprints:R_0603, B.Cu at (212.2, 128.3)
- added R12: 2k2, project_footprints:R_0603, B.Cu at (161.2, 128.3)
- added R12: 2k2, project_footprints:R_0603, B.Cu at (212.2, 94.3)
- added R13: 2k2, project_footprints:R_0603, B.Cu at (212.8, 152.6)
- added R13: 2k2, project_footprints:R_0603, B.Cu at (161.8, 152.6)
- added R13: 2k2, project_footprints:R_0603, B.Cu at (212.8, 118.6)
- added R13: 2k2, project_footprints:R_0603, B.Cu at (161.8, 118.6)
- added R13: 2k2, project_footprints:R_0603, B.Cu at (212.8, 84.6)
- added R14: 1k0, project_footprints:R_0603, B.Cu at (212.0, 177.0)
- added R14: 1k0, project_footprints:R_0603, B.Cu at (161.0, 177.0)
- added R14: 1k0, project_footprints:R_0603, B.Cu at (212.0, 143.0)
- added R14: 1k0, project_footprints:R_0603, B.Cu at (161.0, 143.0)
- added R14: 1k0, project_footprints:R_0603, B.Cu at (212.0, 109.0)
- added R15: 1k0, project_footprints:R_0603, B.Cu at (212.1, 156.9)
- added R15: 1k0, project_footprints:R_0603, B.Cu at (161.1, 156.9)
- added R15: 1k0, project_footprints:R_0603, B.Cu at (212.1, 122.9)
- added R15: 1k0, project_footprints:R_0603, B.Cu at (161.1, 122.9)
- added R15: 1k0, project_footprints:R_0603, B.Cu at (212.1, 88.9)
- added R16: 1k0, project_footprints:R_0603, B.Cu at (211.8, 166.5)
- added R16: 1k0, project_footprints:R_0603, B.Cu at (160.8, 166.5)
- added R16: 1k0, project_footprints:R_0603, B.Cu at (211.8, 132.5)
- added R16: 1k0, project_footprints:R_0603, B.Cu at (160.8, 132.5)
- added R16: 1k0, project_footprints:R_0603, B.Cu at (211.8, 98.5)
- added R17: 560R, project_footprints:R_0603, B.Cu at (212.0, 175.6)
- added R17: 560R, project_footprints:R_0603, B.Cu at (161.0, 175.6)
- added R17: 560R, project_footprints:R_0603, B.Cu at (212.0, 141.6)
- added R17: 560R, project_footprints:R_0603, B.Cu at (161.0, 141.6)
- added R17: 560R, project_footprints:R_0603, B.Cu at (212.0, 107.6)
- added R18: 560R, project_footprints:R_0603, B.Cu at (211.8, 164.9)
- added R18: 560R, project_footprints:R_0603, B.Cu at (160.8, 164.9)
- added R18: 560R, project_footprints:R_0603, B.Cu at (211.8, 130.9)
- added R18: 560R, project_footprints:R_0603, B.Cu at (160.8, 130.9)
- added R18: 560R, project_footprints:R_0603, B.Cu at (211.8, 96.9)
- added R19: 560R, project_footprints:R_0603, B.Cu at (212.8, 154.4)
- added R19: 560R, project_footprints:R_0603, B.Cu at (161.8, 154.4)
- added R19: 560R, project_footprints:R_0603, B.Cu at (212.8, 120.4)
- added R19: 560R, project_footprints:R_0603, B.Cu at (161.8, 120.4)
- added R19: 560R, project_footprints:R_0603, B.Cu at (212.8, 86.4)
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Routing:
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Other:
- board size 49 x 32 mm -> 100 x 100 mm
